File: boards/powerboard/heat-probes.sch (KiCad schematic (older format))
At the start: 16 parts, among them J801 Heat probe power, Q801 N-MOSFET, Q802 N-MOSFET, Q803 N-MOSFET, U801 ACS711, U802 ACS711, U803 ACS711

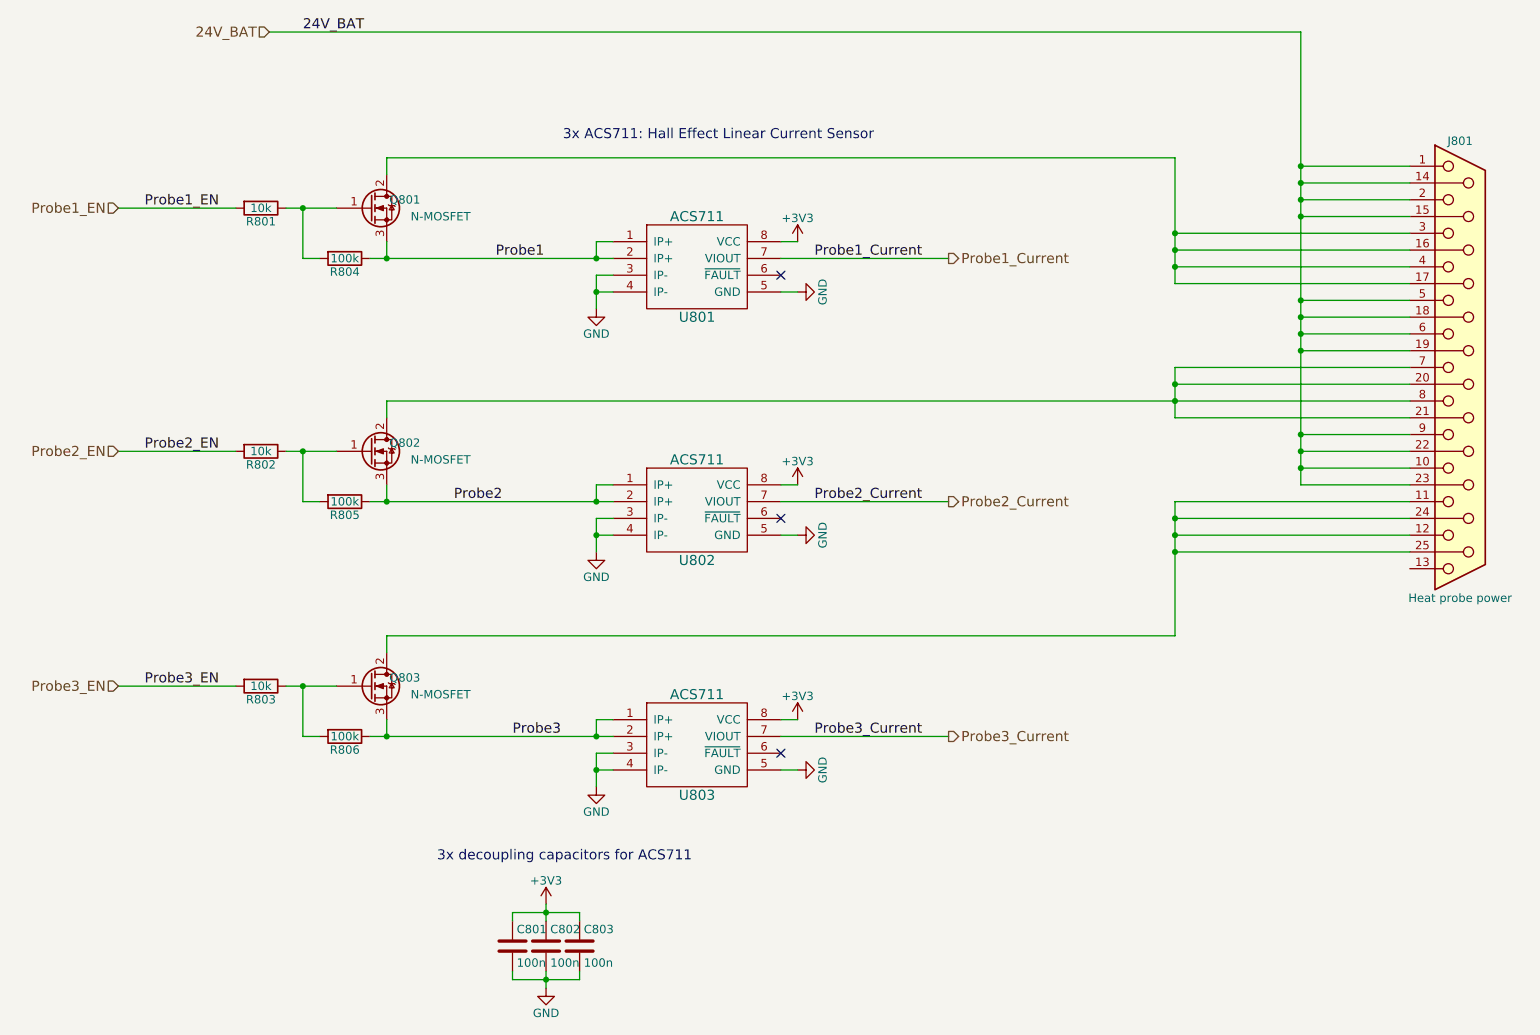
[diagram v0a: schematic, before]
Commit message: [powerboard] LT3757 boost converter(s) on seperate PCB, BLDC motor connector, differential encoder
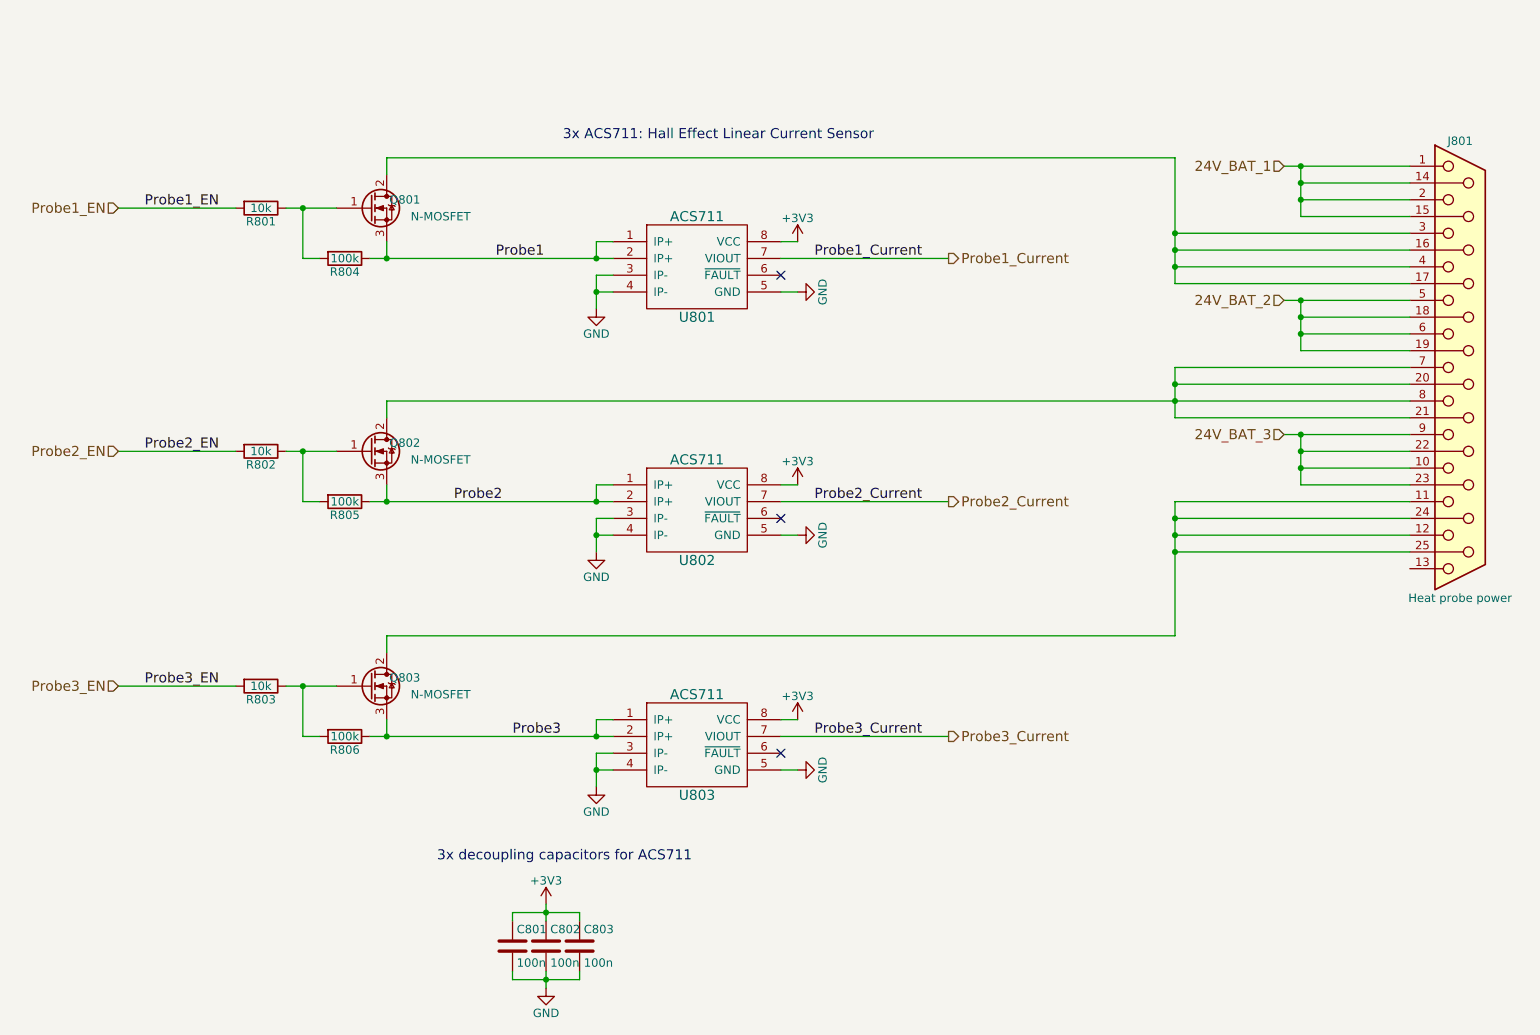
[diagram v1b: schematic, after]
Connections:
- removed net 24V_BAT: J801.1, J801.10, J801.14 (P14), J801.15 (P15), J801.18 (P18), J801.19 (P19), J801.2, J801.22 (P22), J801.23 (P23), J801.5, J801.6, J801.9
- new net 24V_BAT_1: J801.1, J801.14 (P14), J801.15 (P15), J801.2
- new net 24V_BAT_2: J801.18 (P18), J801.19 (P19), J801.5, J801.6
- new net 24V_BAT_3: J801.10, J801.22 (P22), J801.23 (P23), J801.9
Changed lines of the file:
@@
 LIBS:references
 LIBS:lt3592
+LIBS:ds26lv32at
 LIBS:powerboard-cache
 EELAYER 25 0
@@
 $Descr A4 11693 8268
 encoding utf-8
-Sheet 8 11
+Sheet 7 10
 Title "Powerboard: Heat Probes"
 Date "2017-04-15"
@@
 Text Notes 4100 6350 0    60   ~ 0
 3x decoupling capacitors for ACS711
-Text Label 3300 1400 0    60   ~ 0
-24V_BAT
 $Comp
 L Q_NMOS_GDS Q801
@@
 Text Notes 4850 2050 0    60   ~ 0
 3x ACS711: Hall Effect Linear Current Sensor
-Text HLabel 3100 1400 0    60   Input ~ 0
-24V_BAT
-Wire Wire Line
-	3100 1400 9250 1400
+Text HLabel 9150 2200 0    60   Input ~ 0
+24V_BAT_1
 Wire Wire Line
 	3800 2250 3800 2150
@@
 $EndComp
 Wire Wire Line
-	9250 1400 9250 4100
-Wire Wire Line
-	9250 2200 9900 2200
+	9150 2200 9900 2200
 Wire Wire Line
 	9250 2300 9900 2300
@@
 Connection ~ 8500 2800
 Wire Wire Line
-	9250 3000 9900 3000
-Connection ~ 9250 2500
+	9150 3000 9900 3000
 Wire Wire Line
 	9250 3100 9900 3100
@@
 	8500 3700 9900 3700
 Wire Wire Line
-	9250 3800 9900 3800
-Connection ~ 9250 3300
+	9150 3800 9900 3800
 Wire Wire Line
 	9250 3900 9900 3900
@@
 Text HLabel 7150 5600 2    60   Output ~ 0
 Probe3_Current
+Text HLabel 9150 3000 0    60   Input ~ 0
+24V_BAT_2
+Text HLabel 9150 3800 0    60   Input ~ 0
+24V_BAT_3
+Wire Wire Line
+	9250 3000 9250 3300
+Wire Wire Line
+	9250 3800 9250 4100
+Wire Wire Line
+	9250 2200 9250 2500
 $EndSCHEMATC

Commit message: [powerboard] BLDC motor controller
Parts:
- C801, C802, C803: footprint (none) -> Capacitors_SMD:C_0603
- J801: footprint (none) -> Mounting_Holes:MountingHole_3.2mm_M3_Pad_Via
- R801, R802, R803, R804, R805, R806: footprint (none) -> Resistors_SMD:R_0603
- U801, U802, U803: footprint (none) -> Housings_SOIC:SOIC-8_3.9x4.9mm_Pitch1.27mm
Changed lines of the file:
@@
 LIBS:ds26lv32at
 LIBS:drv8312
+LIBS:drv8332
 LIBS:powerboard-cache
 EELAYER 25 0
@@
 F 0 "U801" H 5650 2500 60  0000 C CNN
 F 1 "ACS711" H 5650 3100 60  0000 C CNN
-F 2 "" H 5650 2800 60  0001 C CNN
+F 2 "Housings_SOIC:SOIC-8_3.9x4.9mm_Pitch1.27mm" H 5650 2800 60  0001 C CNN
 F 3 "" H 5650 2800 60  0001 C CNN
 	1    5650 2800
@@
 F 0 "U802" H 5650 3950 60  0000 C CNN
 F 1 "ACS711" H 5650 4550 60  0000 C CNN
-F 2 "" H 5650 4250 60  0001 C CNN
+F 2 "Housings_SOIC:SOIC-8_3.9x4.9mm_Pitch1.27mm" H 5650 4250 60  0001 C CNN
 F 3 "" H 5650 4250 60  0001 C CNN
 	1    5650 4250
@@
 F 0 "U803" H 5650 5350 60  0000 C CNN
 F 1 "ACS711" H 5650 5950 60  0000 C CNN
-F 2 "" H 5650 5650 60  0001 C CNN
+F 2 "Housings_SOIC:SOIC-8_3.9x4.9mm_Pitch1.27mm" H 5650 5650 60  0001 C CNN
 F 3 "" H 5650 5650 60  0001 C CNN
 	1    5650 5650
@@
 F 0 "C801" H 4575 6950 50  0000 L CNN
 F 1 "100n" H 4575 6750 50  0000 L CNN
-F 2 "" H 4588 6700 50  0000 C CNN
+F 2 "Capacitors_SMD:C_0603" H 4588 6700 50  0001 C CNN
 F 3 "" H 4550 6850 50  0000 C CNN
 	1    4550 6850
@@
 F 0 "C802" H 4775 6950 50  0000 L CNN
 F 1 "100n" H 4775 6750 50  0000 L CNN
-F 2 "" H 4788 6700 50  0000 C CNN
+F 2 "Capacitors_SMD:C_0603" H 4788 6700 50  0001 C CNN
 F 3 "" H 4750 6850 50  0000 C CNN
 	1    4750 6850
@@
 F 0 "C803" H 4975 6950 50  0000 L CNN
 F 1 "100n" H 4975 6750 50  0000 L CNN
-F 2 "" H 4988 6700 50  0000 C CNN
+F 2 "Capacitors_SMD:C_0603" H 4988 6700 50  0001 C CNN
 F 3 "" H 4950 6850 50  0000 C CNN
 	1    4950 6850
@@
 F 0 "R801" V 3130 2450 50  0000 C CNN
 F 1 "10k" V 3050 2450 50  0000 C CNN
-F 2 "" V 2980 2450 50  0000 C CNN
+F 2 "Resistors_SMD:R_0603" V 2980 2450 50  0001 C CNN
 F 3 "" H 3050 2450 50  0000 C CNN
 	1    3050 2450
@@
 F 0 "Q802" H 4000 3950 50  0000 R CNN
 F 1 "N-MOSFET" H 4300 3850 50  0000 R CNN
-F 2 "" H 3900 4000 50  0000 C CNN
+F 2 "" H 3900 4000 50  0001 C CNN
 F 3 "" H 3700 3900 50  0000 C CNN
 	1    3700 3900
@@
 F 0 "R802" V 3130 3900 50  0000 C CNN
 F 1 "10k" V 3050 3900 50  0000 C CNN
-F 2 "" V 2980 3900 50  0000 C CNN
+F 2 "Resistors_SMD:R_0603" V 2980 3900 50  0001 C CNN
 F 3 "" H 3050 3900 50  0000 C CNN
 	1    3050 3900
@@
 F 0 "Q803" H 4000 5350 50  0000 R CNN
 F 1 "N-MOSFET" H 4300 5250 50  0000 R CNN
-F 2 "" H 3900 5400 50  0000 C CNN
+F 2 "" H 3900 5400 50  0001 C CNN
 F 3 "" H 3700 5300 50  0000 C CNN
 	1    3700 5300
@@
 F 0 "R803" V 3130 5300 50  0000 C CNN
 F 1 "10k" V 3050 5300 50  0000 C CNN
-F 2 "" V 2980 5300 50  0000 C CNN
+F 2 "Resistors_SMD:R_0603" V 2980 5300 50  0001 C CNN
 F 3 "" H 3050 5300 50  0000 C CNN
 	1    3050 5300
@@
 F 0 "R804" V 3630 2750 50  0000 C CNN
 F 1 "100k" V 3550 2750 50  0000 C CNN
-F 2 "" V 3480 2750 50  0000 C CNN
+F 2 "Resistors_SMD:R_0603" V 3480 2750 50  0001 C CNN
 F 3 "" H 3550 2750 50  0000 C CNN
 	1    3550 2750
@@
 F 0 "R805" V 3630 4200 50  0000 C CNN
 F 1 "100k" V 3550 4200 50  0000 C CNN
-F 2 "" V 3480 4200 50  0000 C CNN
+F 2 "Resistors_SMD:R_0603" V 3480 4200 50  0001 C CNN
 F 3 "" H 3550 4200 50  0000 C CNN
 	1    3550 4200
@@
 F 0 "R806" V 3630 5600 50  0000 C CNN
 F 1 "100k" V 3550 5600 50  0000 C CNN
-F 2 "" V 3480 5600 50  0000 C CNN
+F 2 "Resistors_SMD:R_0603" V 3480 5600 50  0001 C CNN
 F 3 "" H 3550 5600 50  0000 C CNN
 	1    3550 5600
@@
 F 0 "Q801" H 4000 2500 50  0000 R CNN
 F 1 "N-MOSFET" H 4300 2400 50  0000 R CNN
-F 2 "" H 3900 2550 50  0000 C CNN
+F 2 "" H 3900 2550 50  0001 C CNN
 F 3 "" H 3700 2450 50  0000 C CNN
 	1    3700 2450
@@
 F 0 "J801" H 10200 4750 50  0000 C CNN
 F 1 "Heat probe power" H 10200 2025 50  0000 C CNN
-F 2 "" H 10200 3400 50  0001 C CNN
+F 2 "Mounting_Holes:MountingHole_3.2mm_M3_Pad_Via" H 10200 3400 50  0001 C CNN
 F 3 "" H 10200 3400 50  0001 C CNN
 	1    10200 3400

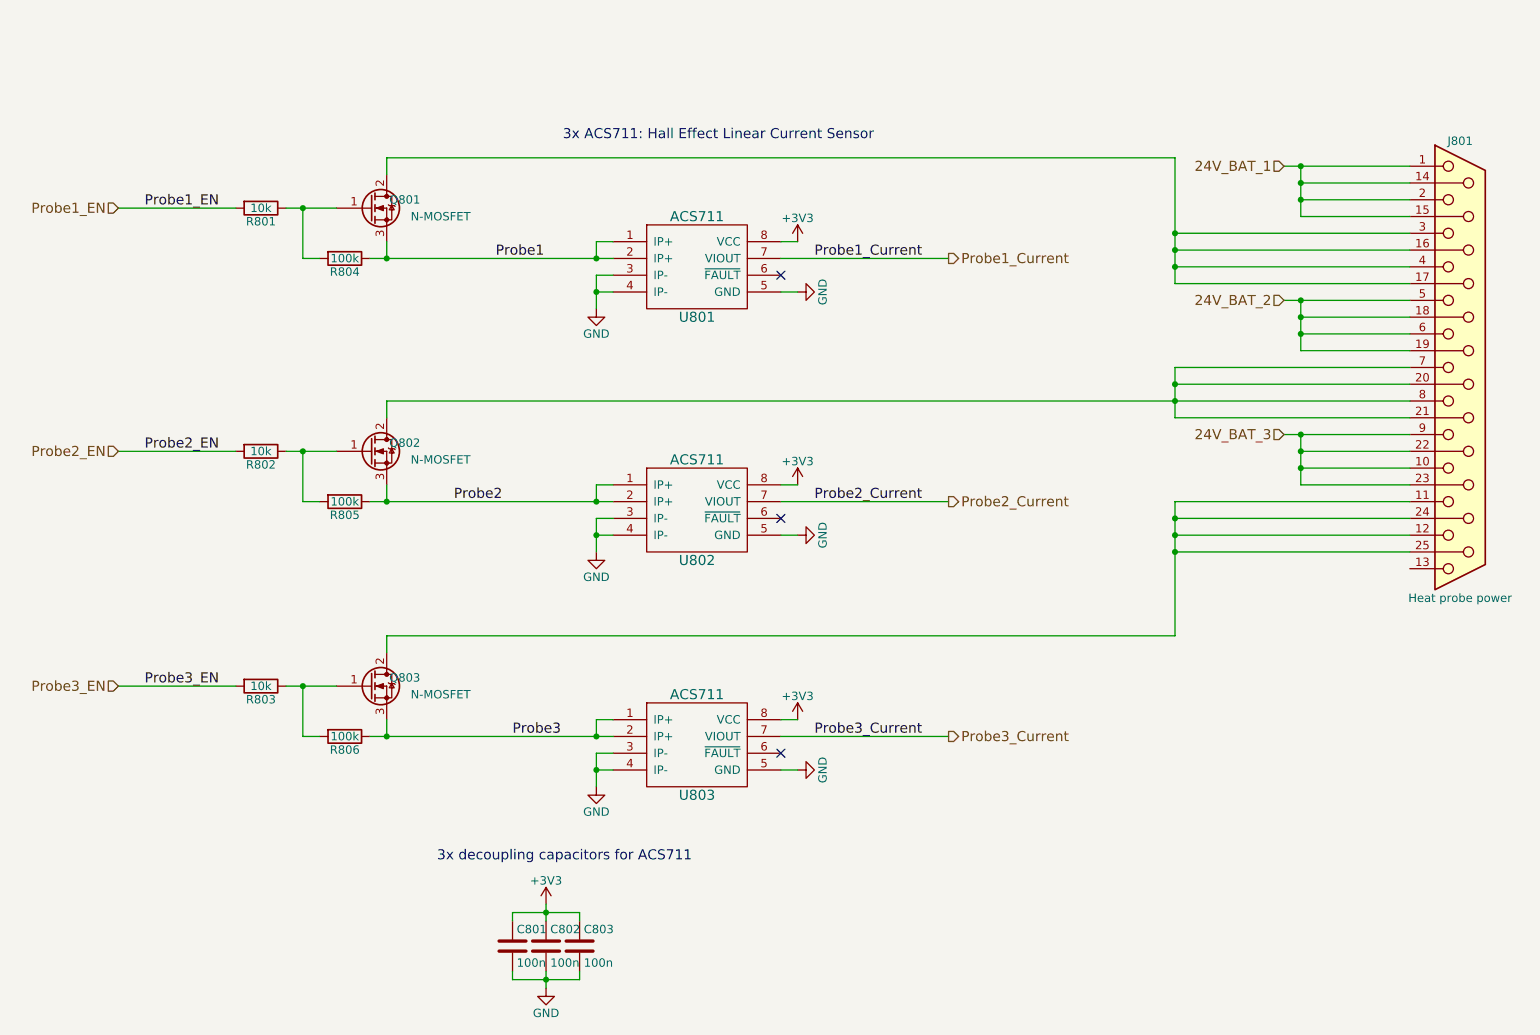
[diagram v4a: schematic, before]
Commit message: [powerboard] selected all components and assigned all footprints
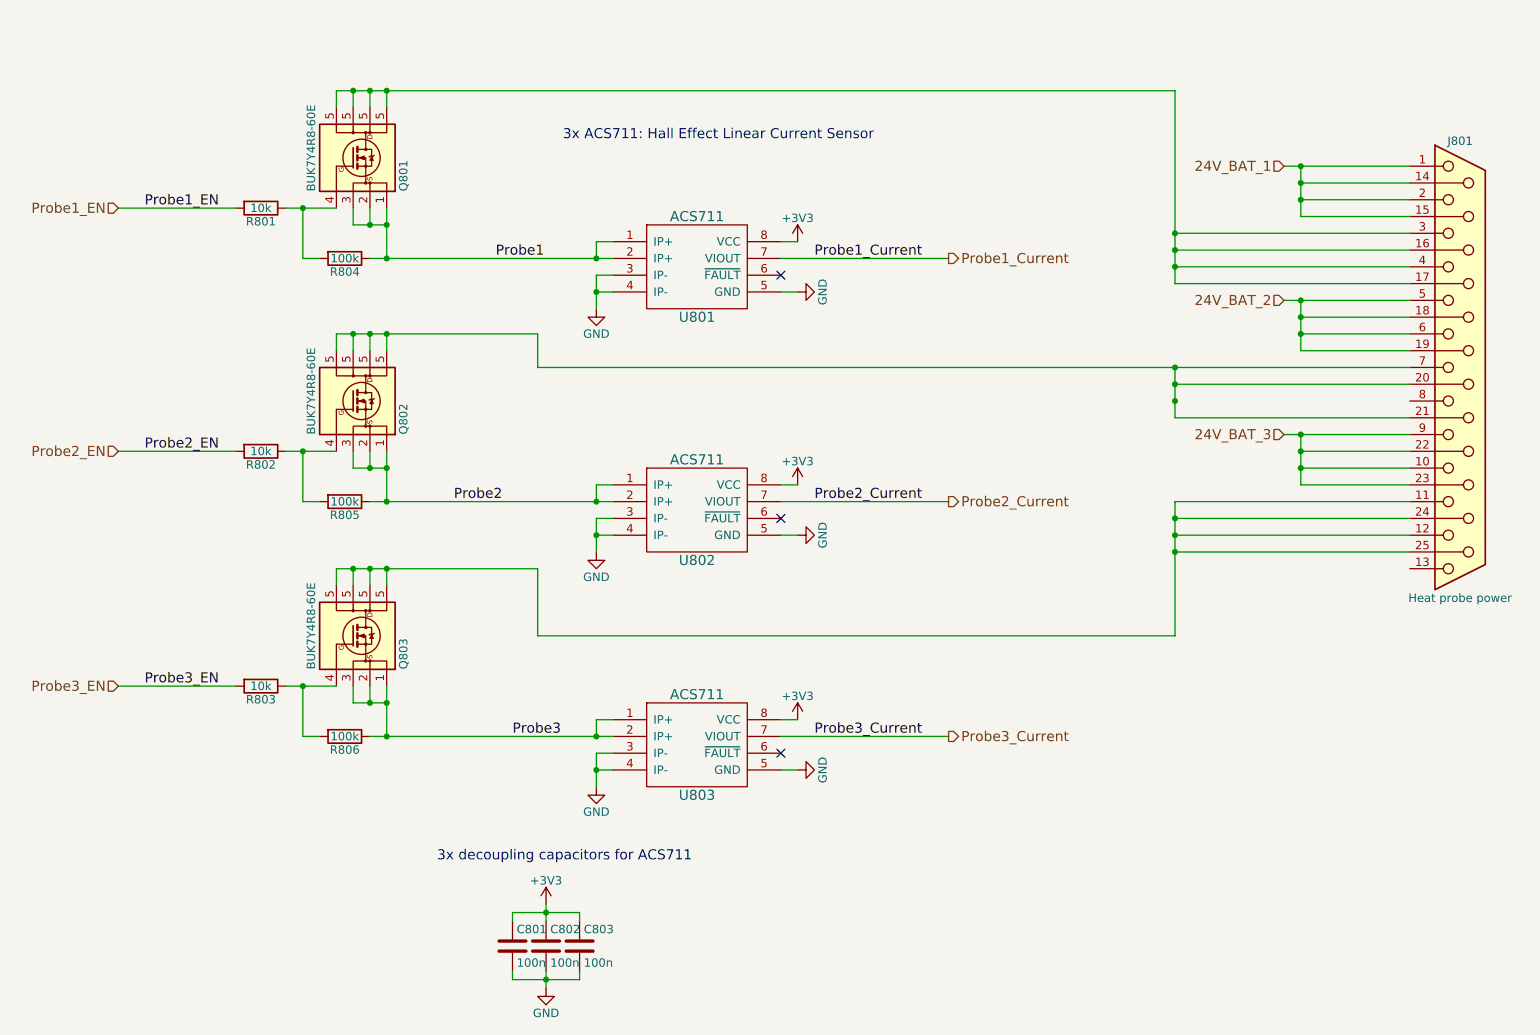
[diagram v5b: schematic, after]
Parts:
- removed Q801, Q802, Q803: N-MOSFET, symbol Q_NMOS_GDS
- added Q801, Q802, Q803: BUK7Y4R8-60E, TO_SOT_Packages_SMD:SOT-669_LFPAK, symbol CSD17501Q5A
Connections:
- net Probe1: now also Q801.1 (S), Q801.2 (S), Q801.3 (S)
- net Probe2: now also Q802.1 (S), Q802.2 (S), Q802.3 (S)
- net Probe3: now also Q803.1 (S), Q803.2 (S), Q803.3 (S)
- net at R801.1, R804.2: now also Q801.4 (G)
- net at J801.16 (P16), J801.17 (P17), J801.3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: now also Q801.5 (D)
- net at R802.1, R805.2: now also Q802.4 (G)
- net at J801.20 (P20), J801.21 (P21), J801.7: now also Q802.5 (D); no longer J801.8
- net at R803.1, R806.2: now also Q803.4 (G)
- net at J801.11, J801.12, J801.24 (P24)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: now also Q803.5 (D)
